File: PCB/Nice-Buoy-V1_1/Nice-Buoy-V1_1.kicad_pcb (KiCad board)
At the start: 4 copper layers, 100 x 80 mm, 160 parts, among them J101 1051330011, J102 Display, J103 LEDSTRIP, J104 SW1, J105 SW2, J201 Accu, J202 ESC SB POWER, J203 ESC BB POWER, J401 ESC-BB, J402 ESC-SB, J501 GPS, J601 Conn_Coaxial, J701 LED1, J702 LED2, J703 LED3, J704 SW1, J705 SW3, J706 SW2, J707 3.3V switch, J708 Vbatt switch, J709 MainswitchLeds, J901 Display, Q101 2N7002, Q102 2N7002, Q201 NCE01P30K, Q701 MMBT5551L, Q702 MMBT5551L, Q703 MMBT5551L, Q704 MMBT5551L, SW101 ~{BOOT}, SW102 ~{RESET}, SW201 ON/OFF, U101 SRV05-4, U102 CP2104-F03-GMR, U103 ESP32-WROOM-32E_(visible_peri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, U201 AP7363, U202 XL1509-5.0E1, U301 LSM303C, U601 Ai-Thinker-Ra-01, U701 MCP23017_SS, U801 LIS2HH12

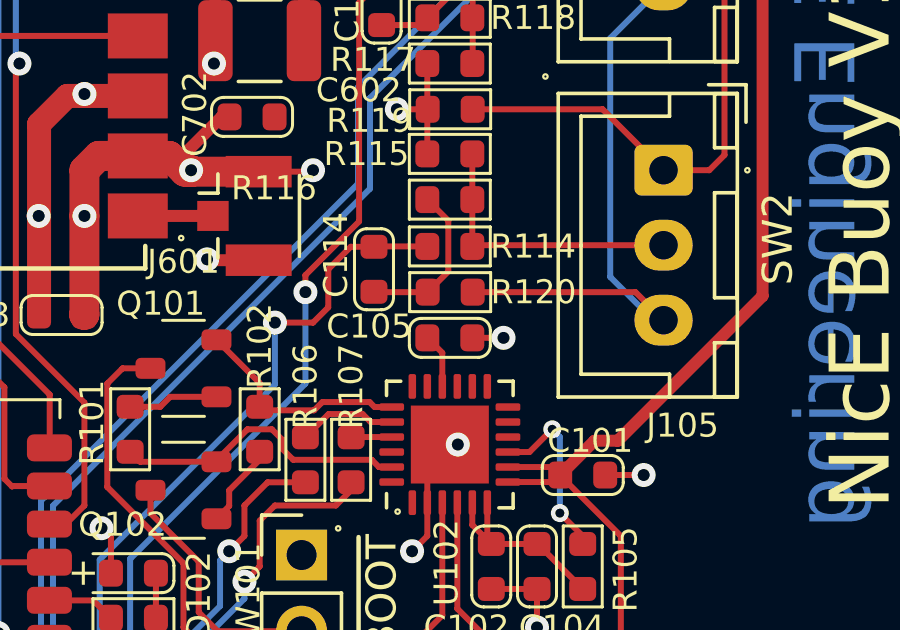
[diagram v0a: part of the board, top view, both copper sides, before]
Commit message: settingup V1.1 software. Compasso ok dispay ok gps ok
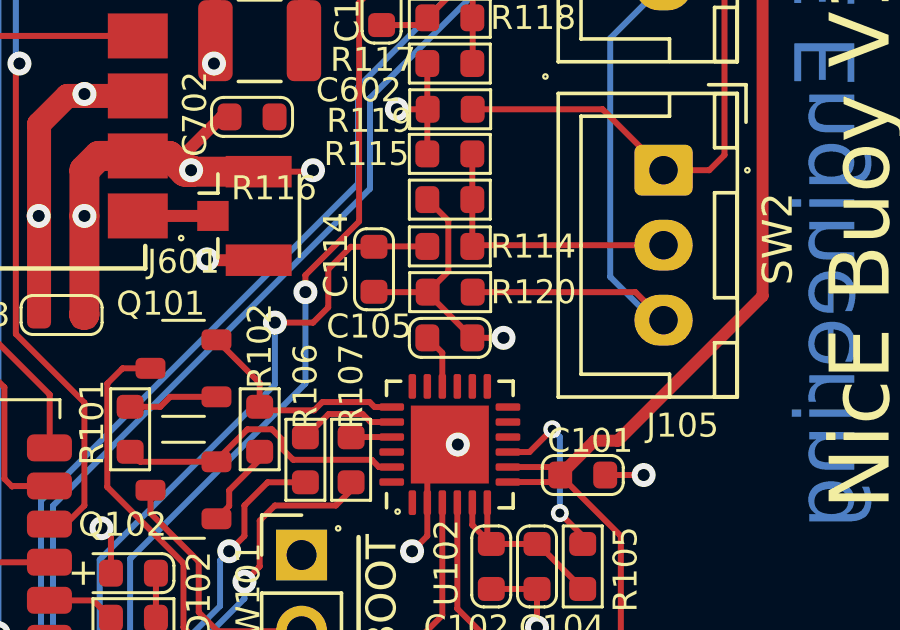
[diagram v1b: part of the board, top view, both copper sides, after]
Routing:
- net GND: track 338.8 -> 340.9 mm
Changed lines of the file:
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@@
   (segment (start 114.22 113.727) (end 114.983 113.727) (width 1) (layer "F.Cu") (net 2))
   (segment (start 79.378 98.372) (end 79.507 98.372) (width 0.2) (layer "F.Cu") (net 2))
+  (segment (start 126.818 92.022) (end 126.818 92.058) (width 0.2) (layer "F.Cu") (net 2))
   (segment (start 88.51 81.14) (end 88.51 82.39) (width 0.2) (layer "F.Cu") (net 2))
   (segment (start 113.783 42.17) (end 117.218 38.735) (width 0.8) (layer "F.Cu") (net 2))
@@
   (segment (start 68.452 103.7845) (end 67.5455 103.7845) (width 0.25) (layer "F.Cu") (net 2))
   (segment (start 81.277 43.307) (end 81.531 43.561) (width 1) (layer "F.Cu") (net 2))
+  (segment (start 126.818 92.058) (end 128.306 93.546) (width 0.2) (layer "F.Cu") (net 2))
   (segment (start 118.424 87.704) (end 118.727 88.007) (width 1) (layer "F.Cu") (net 2))
   (segment (start 118.202 87.482) (end 118.424 87.704) (width 1) (layer "F.Cu") (net 2))
